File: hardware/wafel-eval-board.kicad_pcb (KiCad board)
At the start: 2 copper layers, 264 parts, among them J101 CAN PORT, J102 SW, J201 Conn_01x02, J202 Conn_01x02, J203 Conn_01x02, J204 Conn_01x02, J205 Conn_01x02, J801 UART1, Q1001 CJ3134K, Q101 AO3422, Q1101 CJ3134K, Q1201 CJ3134K, Q1301 CJ3134K, Q1401 CJ3134K, Q1501 CJ3134K, Q1601 CJ3134K, Q1701 CJ3134K, Q1801 CJ3134K, Q1901 CJ3134K, Q201 NPN, Q202 2N7002K, Q301 IRLML6402, Q302 2N7002K, Q401 IPB085N15NM6, Q402 IPB085N15NM6, Q403 IPB085N15NM6, Q501 IPB085N15NM6, Q502 IPB085N15NM6, Q503 IPB085N15NM6, Q601 IRFR9024, Q701 IRFR9024, Q901 ZXMP10A13FTA, Q902 2N7002K, SW801 SW_Push, U101 LM5163DDA, U201 BQ7694204, U801 NUCLEO-L432KC, U802 TCAN1043A, U803 TLP241A

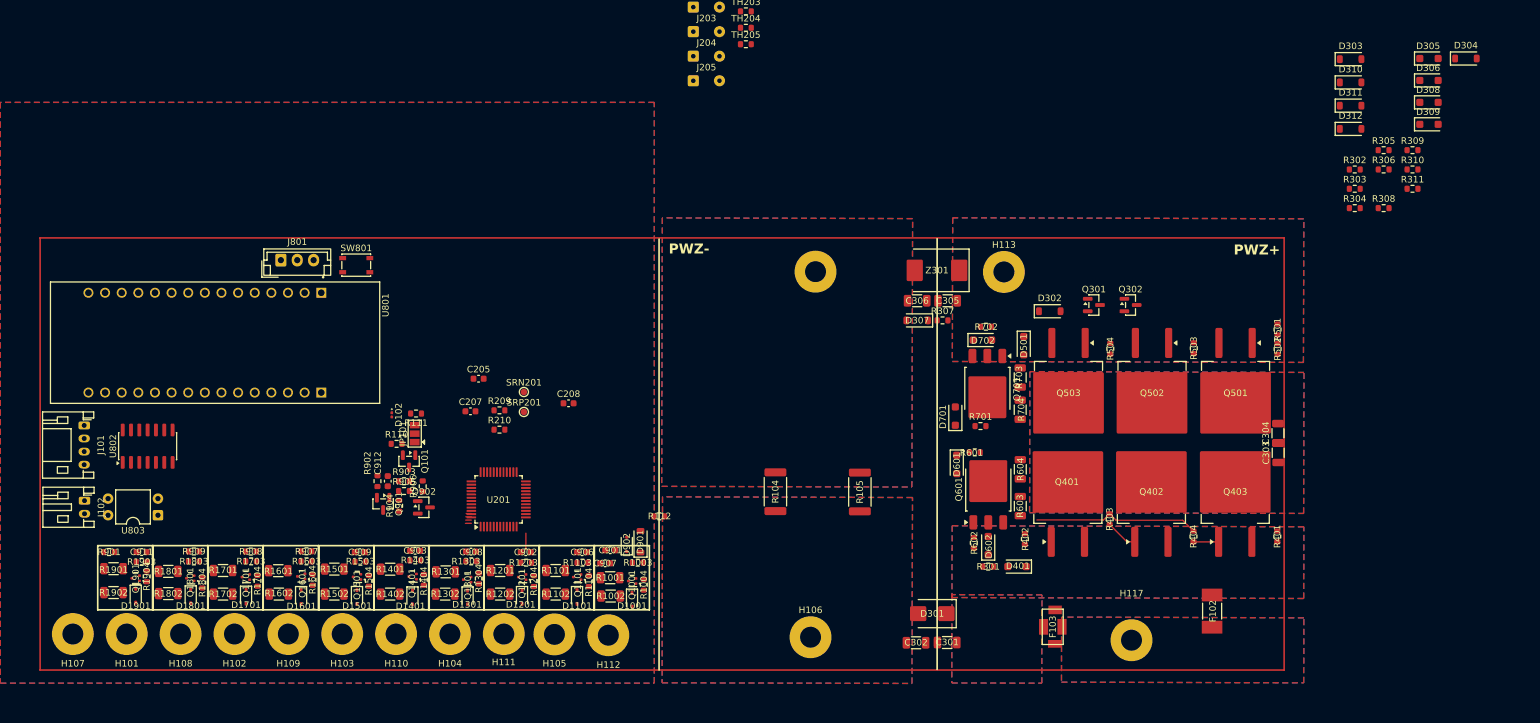
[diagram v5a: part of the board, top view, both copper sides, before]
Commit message: Sync PCB layout with updated schematic footprints (Q601/Q701 to SOT-23, C301-C306 to 1206)
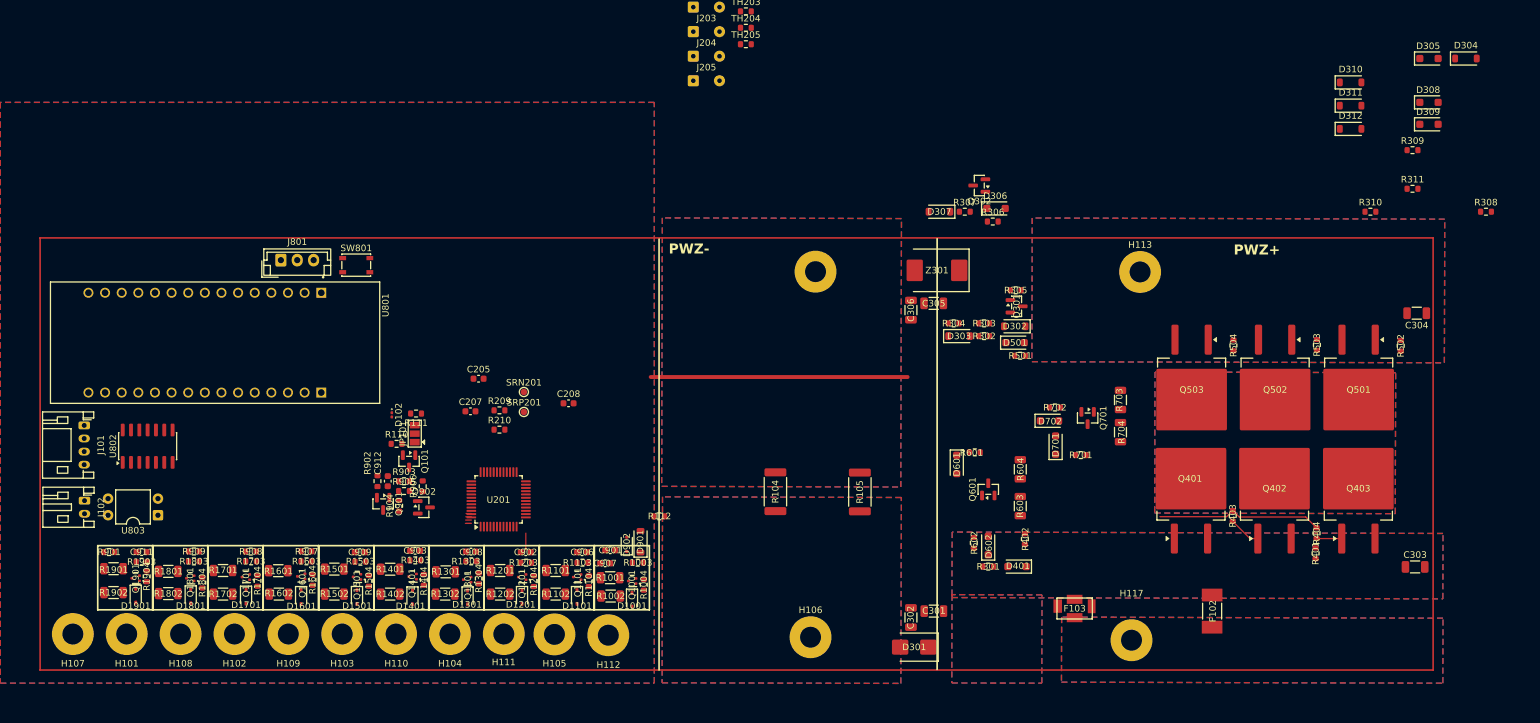
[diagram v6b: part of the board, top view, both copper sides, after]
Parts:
- Q601, Q701: value IRFR9024 -> PJM10H01PSA; footprint Package_TO_SOT_SMD:TO-252-3_TabPin2 -> Package_TO_SOT_SMD:SOT-23
- R402, R403, R404, R502, R503, R504, R601, R701: value 51 -> 600R
- moved D303 73.3 mm to (198.3, 61.0)
- moved D306 68.9 mm to (204.0, 41.5)
- moved R304 63.7 mm to (197.5, 59.0), turned to 180 degrees
- moved R302 62.1 mm to (202.2, 61.0), turned to 180 degrees
- moved R303 60.2 mm to (202.2, 59.0), turned to 180 degrees
- moved R306 60.2 mm to (203.5, 43.5)
- moved R305 60.1 mm to (207.0, 54.0), turned to 180 degrees
- moved R501 39.5 mm to (207.7, 64.0), turned to 0 degrees
- moved Q302 29.4 mm to (201.4, 38.0), turned to 180 degrees
- moved C304 28.0 mm to (268.2, 57.5), turned to 180 degrees
- moved C303 27.2 mm to (268.0, 96.2), turned to 0 degrees
- moved H113 20.8 mm to (226.0, 51.2)
- moved Q402 18.8 mm to (246.5, 84.3)
- moved Q502 18.8 mm to (246.6, 69.2)
- moved R404 18.8 mm to (252.9, 91.1)
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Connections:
- F103 pad 1: /xBAT+ -> /BAT+
- F103 pad 3: /BAT+ -> /xBAT+
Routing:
- net GND: track 0.00 -> 39.2 mm

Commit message: Shrink load dump Schottky diodes to SOD-323 (BAT46WS)
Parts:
- moved H114 287.5 mm to (293.2, 77.8)
- moved C206 135.1 mm to (119.5, 87.8), turned to 90 degrees
- moved R110 96.2 mm to (206.2, 98.8), turned to 90 degrees
- moved R312 95.0 mm to (215.7, 83.6)
- moved Q101 91.0 mm to (203.6, 98.3)
- moved D102 90.7 mm to (199.7, 94.9), turned to 0 degrees
- moved JP101 89.8 mm to (202.9, 94.8), turned to 180 degrees
- moved D304 87.0 mm to (203.7, 67.4), turned to 180 degrees
- moved D308 85.9 mm to (205.5, 81.8), turned to 90 degrees
- moved R111 84.6 mm to (197.1, 94.8), turned to 0 degrees
- moved D305 81.0 mm to (203.7, 64.9), turned to 180 degrees
- moved D309 80.0 mm to (205.4, 75.6), turned to -90 degrees
- moved R309 77.5 mm to (209.2, 83.6)
- moved D310 77.1 mm to (209.0, 81.6), turned to 180 degrees
- moved R308 76.8 mm to (209.2, 74.2)
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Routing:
- net /Frontend/DSG: track 0.00 -> 92.8 mm
- net /Frontend/CHG: track 0.86 -> 85.8 mm
- net /Frontend/PACK: track 0.00 -> 83.2 mm
- net /Frontend/LD: track 0.00 -> 81.6 mm
- net /Frontend/PCHG: track 0.00 -> 80.6 mm
- net /Frontend/PDSG: track 0.00 -> 79.1 mm
- net /FUSE: track 0.00 -> 77.5 mm
- net GND: track 39.2 -> 2.60 mm
- net Net-(D306-K): track 0.00 -> 11.6 mm
- net /High-Side N-MOSFET/MOSFET-CASCADE-DSG/GATE: track 0.00 -> 9.07 mm
- net Net-(D302-A): track 0.00 -> 6.32 mm
- net Net-(Q101-D): track 0.00 -> 4.52 mm
- net Net-(U201-CP1): track 0.91 -> 4.65 mm
- net /Frontend/BAT: track 0.80 -> 4.50 mm
- net Net-(D303-A): track 0.00 -> 2.69 mm
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
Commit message: Sync PCB layout with updated gate ferrite bead symbols
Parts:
- D310, D311, D312: value BAT46W -> BAT46WS; footprint Diode_SMD:D_SOD-123 -> Diode_SMD:D_SOD-323
- moved C211 228.8 mm to (100.8, -27.2)
- moved C212 228.8 mm to (100.8, -24.2)
- moved C213 228.8 mm to (105.2, -30.2)
- moved C214 228.8 mm to (105.2, -27.2)
- moved C215 228.8 mm to (105.2, -24.2)
- moved D201 228.8 mm to (98.2, -15.7)
- moved Q202 228.8 mm to (105.0, -20.5)
- moved C204 228.8 mm to (96.3, -30.2)
- moved CP201 228.8 mm to (108.0, -16.7)
- moved D202 228.8 mm to (104.5, -16.4)
- moved F201 228.8 mm to (98.3, -20.3)
- moved R203 228.8 mm to (91.9, -30.2)
- moved R204 228.8 mm to (91.9, -27.3)
- moved R205 228.8 mm to (91.9, -24.4)
- moved R206 228.8 mm to (91.9, -21.4)
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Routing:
- net /High-Side N-MOSFET/MOSFET-CASCADE-DSG/GATE: track 9.07 -> 73.0 mm
- net /PACK+: track 0.02 -> 40.6 mm
- net Net-(C303-Pad2): track 0.00 -> 38.9 mm
- net /CH: track 6.07 -> 41.7 mm
- net Net-(U201-SRP): track 0.00 -> 33.3 mm
- net Net-(U201-SRN): track 0.00 -> 31.5 mm
- net /High-Side N-MOSFET/MOSFET-CASCADE-CHG/GATE: track 25.4 -> 55.1 mm
- net /Frontend/PDSG: track 79.1 -> 102.2 mm
- net /Frontend/PCHG: track 80.6 -> 99.7 mm
- net /FUSE: track 77.5 -> 94.1 mm
- net /Frontend/CHG: track 85.8 -> 102.1 mm
- net Net-(D306-K): track 11.6 -> 25.3 mm
- net /BAT+: track 0.00 -> 12.3 mm
- net PGND: track 0.00 -> 11.1 mm
- net Net-(F103-Pad4): track 0.00 -> 8.00 mm
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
